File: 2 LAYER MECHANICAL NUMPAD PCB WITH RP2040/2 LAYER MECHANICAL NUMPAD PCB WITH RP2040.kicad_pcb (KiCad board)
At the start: 2 copper layers, 76.2 x 101.6 mm, 93 parts, among them IC2 RP2040_QFN56, J1 USB_C_Receptacle_USB2.0_16P, SW1 SW_Push, SW10 SW_Push, SW11 SW_Push, SW12 SW_Push, SW13 SW_Push, SW14 SW_Push, SW15 SW_Push, SW16 SW_Push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

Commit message: Created files
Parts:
- D31, D32, D33, D34, D35, D36, D37, D38, D39, D40, D41, D42, D43, D44, D45, D46, D47, D48, D49, D50: footprint LED_SMD:LED_SK6812MINI-E_3.2x2.8mm_P1.5mm_ReverseMount -> JH_FOOTPRINTS:LED_SK6812MINI-E_3.2x2.8mm_P1.5mm_ReverseMount
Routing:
- net VBUS: track 523.8 -> 516.4 mm, vias 35 -> 34
- net Net-(D41-DOUT): track 98.4 -> 96.3 mm
- net /D9: track 38.0 -> 39.9 mm
- net /NEOSIG: track 64.5 -> 65.5 mm
- net /ROW1: track 117.9 -> 118.5 mm
- net /ROW3: track 87.5 -> 88.1 mm
- net /COL2: track 105.6 -> 106.1 mm
- net /ROW2: track 123.1 -> 123.4 mm, vias 4 -> 3
- net GND: vias 87 -> 90

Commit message: Finalized PCB design
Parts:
- moved C8 0.48 mm to (86.5, 24.5)
- moved D48 0.43 mm to (32.8, 26.7)
- moved D49 0.43 mm to (38.3, 26.7)
- moved D50 0.43 mm to (43.7, 26.7)
- moved C9 0.41 mm to (100.7, 87.8)
- moved C15 0.40 mm to (101.1, 90.7)
- moved D40 0.36 mm to (76.2, 80.6)
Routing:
- net Net-(D37-DOUT): track 60.4 -> 68.1 mm
- net Net-(D44-DOUT): track 48.5 -> 55.6 mm
- net VBUS: track 516.4 -> 521.3 mm
- net /USB_BOOT: track 64.0 -> 66.0 mm
- net /COL2: track 106.1 -> 108.1 mm
- net /ROW2: track 123.4 -> 124.8 mm
- net /D-: track 73.4 -> 74.8 mm
- net Net-(D46-DOUT): track 19.8 -> 21.2 mm
- net Net-(J1-CC2): track 12.9 -> 14.2 mm
- net /COL3: track 95.5 -> 96.7 mm
- net Net-(D47-DOUT): track 180.0 -> 181.1 mm
- net Net-(IC2-USB_D-): track 18.8 -> 19.7 mm
- net 3.3V: track 151.5 -> 152.3 mm, vias 19 -> 18
- net /ROW1: track 118.5 -> 119.3 mm
- net Net-(IC2-XIN): track 9.34 -> 10.1 mm
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
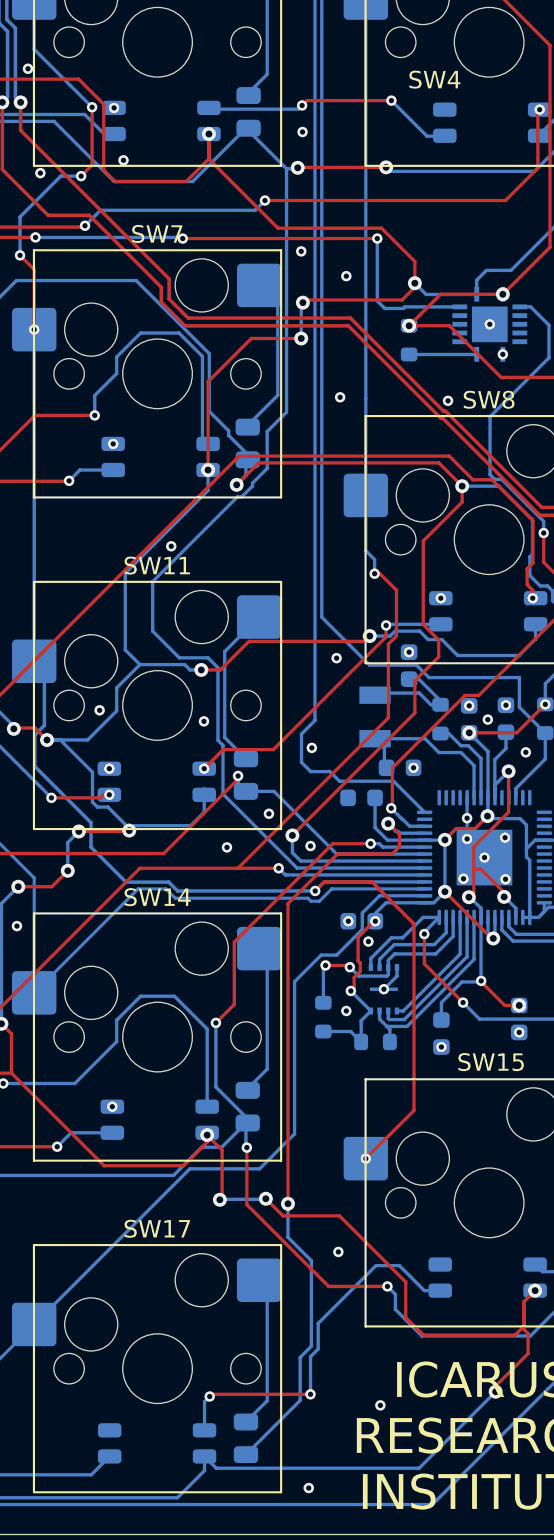
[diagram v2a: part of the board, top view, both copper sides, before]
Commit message: Finalized PCB and ordered 3X PCBs, 1X solder stencil, solder paste, and various components
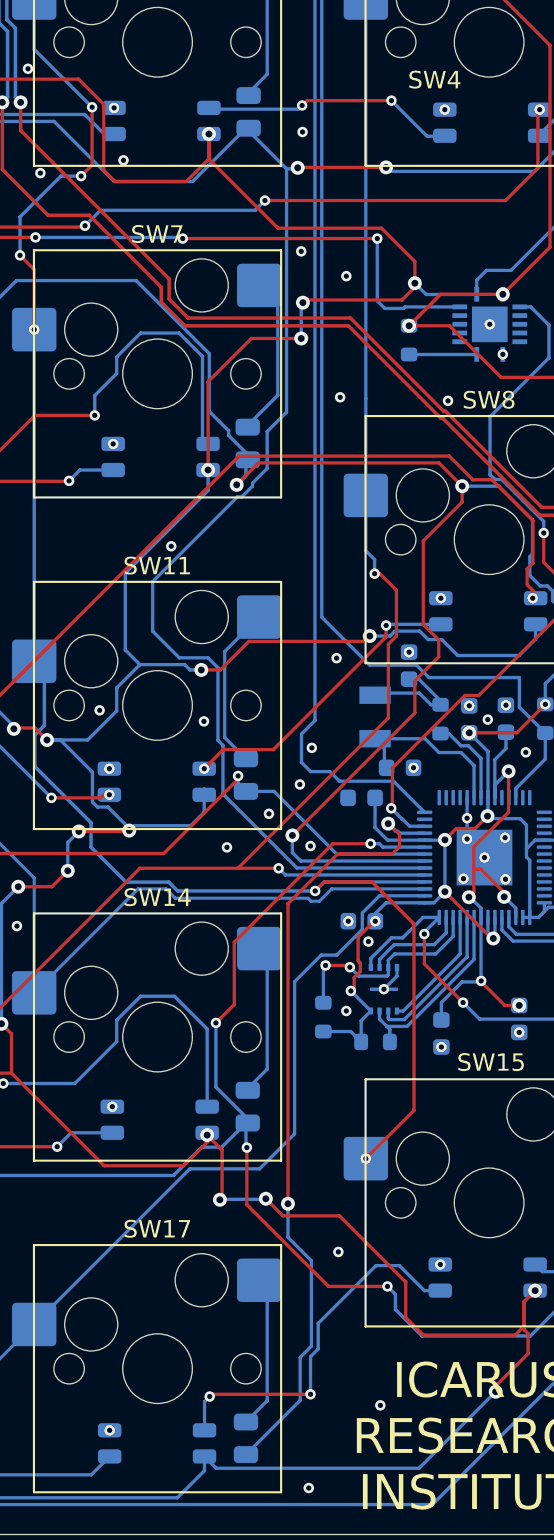
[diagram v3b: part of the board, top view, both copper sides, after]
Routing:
- net GND: vias 96 -> 100
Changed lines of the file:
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@@
 			(drillshape 0)
 			(scaleselection 1)
-			(outputdirectory "GERBERS 2026-06-18/")
+			(outputdirectory "GERBERS 2026-06-22/")
 		)
 	)
@@
 	)
 	(via
+		(at 92.4416 108.3176)
+		(size 0.6)
+		(drill 0.3)
+		(layers "F.Cu" "B.Cu")
+		(net "GND")
+	)
+	(via
 		(at 57.3156 24.4602)
 		(size 0.6)
@@
 	)
 	(via
+		(at 92.7028 41.9728)
+		(size 0.6)
+		(drill 0.3)
+		(layers "F.Cu" "B.Cu")
+		(net "GND")
+	)
+	(via
 		(at 30.3022 64.6938)
 		(size 0.6)
@@
 	)
 	(via
+		(at 84.377715 80.739144)
+		(size 0.6)
+		(drill 0.3)
+		(layers "F.Cu" "B.Cu")
+		(free yes)
+		(net "GND")
+	)
+	(via
 		(at 95.1738 77.0128)
 		(size 0.6)
@@
 		(size 0.6)
 		(drill 0.3)
+		(layers "F.Cu" "B.Cu")
+		(net "GND")
+	)
+	(via
+		(at 73.4496 117.8426)
+		(size 0.6)
+		(drill 0.3)
